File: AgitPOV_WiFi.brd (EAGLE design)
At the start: 36.2 x 66 mm, 33 parts

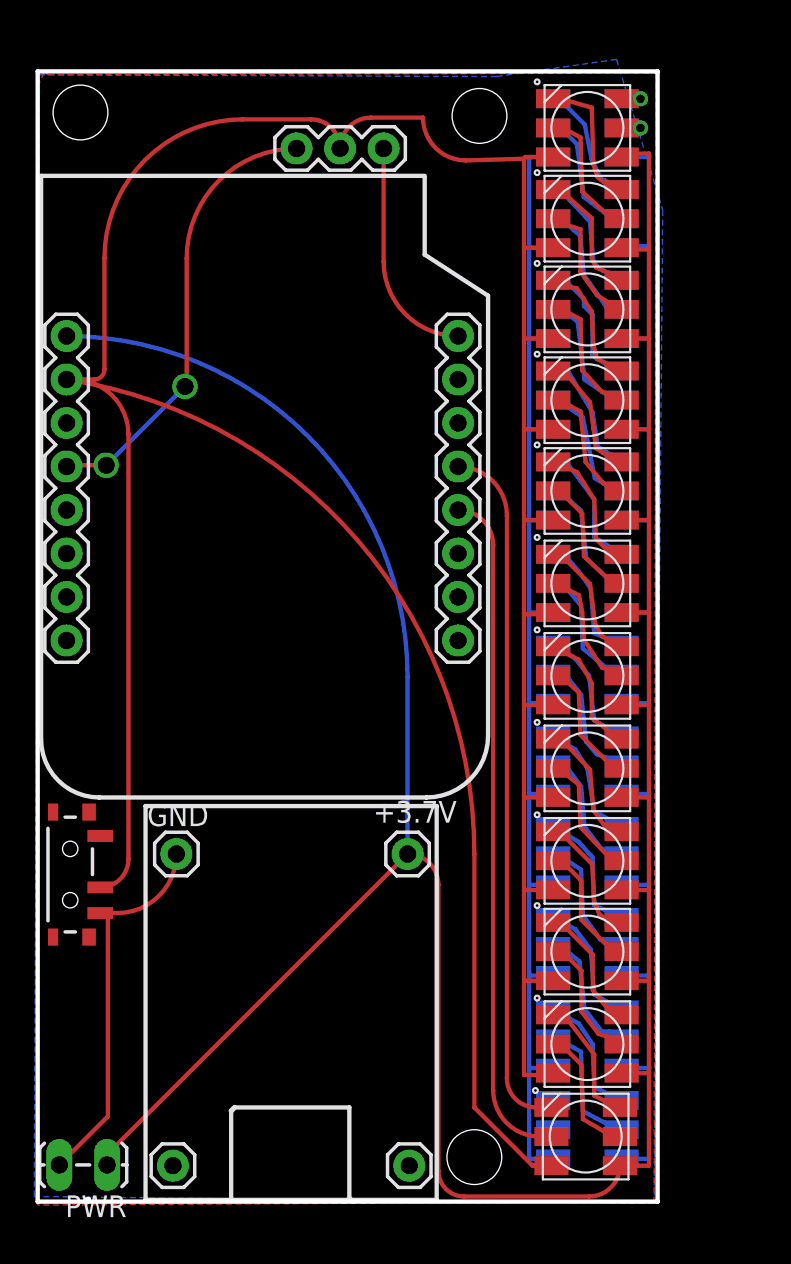
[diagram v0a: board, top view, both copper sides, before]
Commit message: With an option (untested) of an accelerometer.
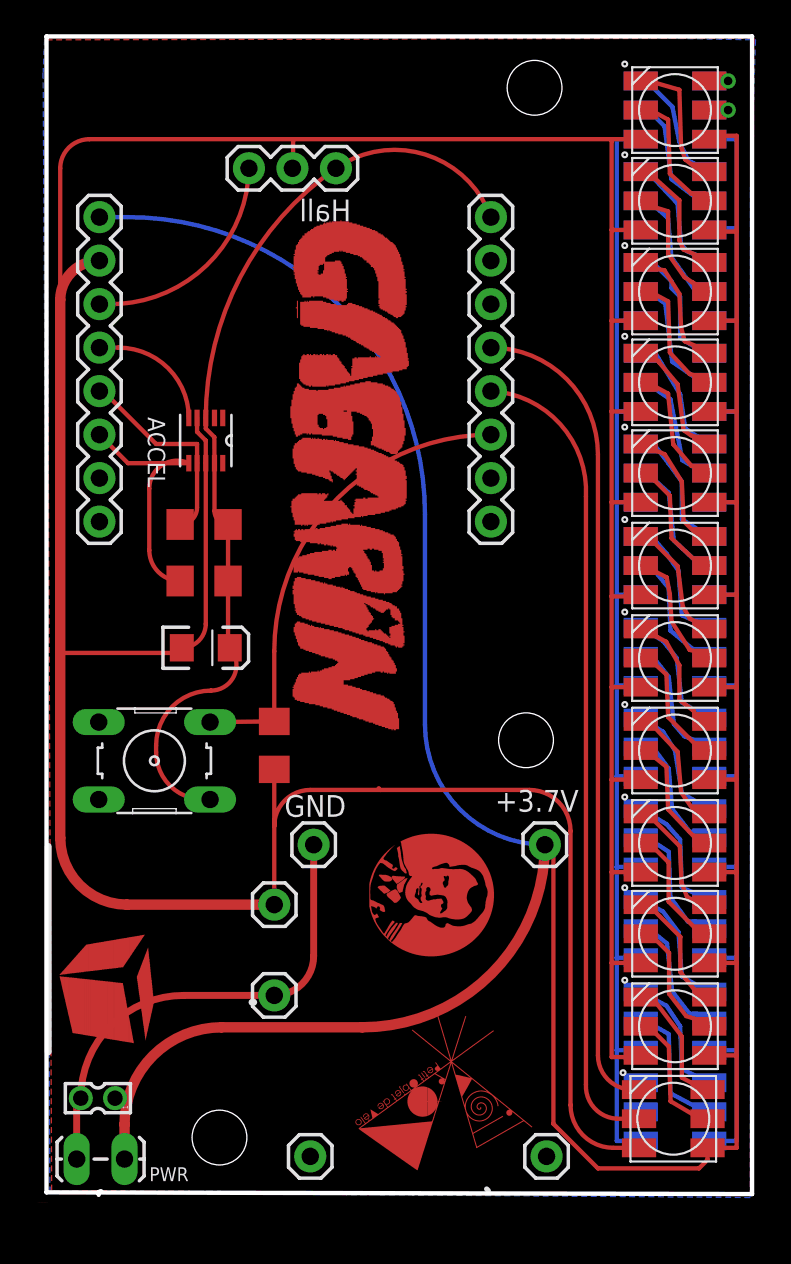
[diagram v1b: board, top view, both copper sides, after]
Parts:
- removed S1: (no value), SparkFun-Electromechanical:SWITCH-SPST-SMD-A
- added ACCEL: MMA7660FCT, Freescale_By_element14_Batch_1:DFN300X300X100-10N
- added C1: 0.1uF, SparkFun-Capacitors:EIA3216
- added JP3: SWITCH, SparkFun-Connectors:1X01
- added JP4: -, SparkFun-Connectors:1X01
- added JST: 332-02, con-garry:332-02
- added PUSHBUTTON: (no value), switch-omron:B3F-10XX
- added R1, R2: 4.7k, SparkFun-Resistors:1206
- added R3: 10k, SparkFun-Resistors:1206
- moved PIN0 8.03 mm to (29.7, 2.64)
- moved GND 8.03 mm to (16.1, 20.8)
- moved KK 8.03 mm to (15.9, 2.64)
- moved +3.7V 8.03 mm to (29.6, 20.8)
- moved WEMOS1 7.20 mm to (26.5, 39.7)
- moved WEMOS2 7.20 mm to (3.61, 57.5)
- moved DEL1 5.22 mm to (37.1, 4.84)
- moved DEL11 5.22 mm to (37.2, 58.4)
- moved DEL16 5.22 mm to (37.2, 47.8)
- moved DEL19 5.22 mm to (37.2, 31.8)
- moved DEL2 5.22 mm to (37.2, 10.2)
- moved DEL20 5.22 mm to (37.2, 26.5)
- moved DEL21 5.22 mm to (37.2, 21.2)
- moved DEL22 5.22 mm to (37.2, 15.9)
- moved DEL23 5.22 mm to (37.2, 10.5)
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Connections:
- removed net CH_PD: HALL.1, WEMOS1.8
- removed net D3: HALL.3, WEMOS2.4
- new net +3.3V: ACCEL.3, ACCEL.9, C1.A, HALL.1, PUSHBUTTON.1, R1.2, R2.2, WEMOS1.8
- new net N$1: HALL.3, WEMOS2.3
- new net N$5: ACCEL.6, R2.1, WEMOS2.6
- new net N$65: ACCEL.7, R1.1, WEMOS2.5
- new net N$67: ACCEL.5, WEMOS2.4
- new net PULLDOWN: PUSHBUTTON.3, R3.2, WEMOS1.3
- net 5V: now also JST.1
- net GND: now also ACCEL.4, ACCEL.8, C1.C, JP3.1, R3.1; no longer S1.2
- net N$41: now also JP4.1, JST.2; no longer S1.1
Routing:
- net +3.3V: track 0.00 -> 51.9 mm
- net GND: track 201.0 -> 233.8 mm
- net PULLDOWN: track 0.00 -> 25.7 mm
- net D3: track 25.5 -> 0.00 mm, vias 2 -> 0
- net 5V: track 173.8 -> 191.3 mm
- net N$5: track 0.00 -> 14.8 mm
- net CH_PD: track 12.8 -> 0.00 mm
- net N$65: track 0.00 -> 12.1 mm
- net N$1: track 0.00 -> 11.9 mm
- net N$2: track 39.3 -> 46.6 mm
- net N$4: track 40.2 -> 47.1 mm
- net N$67: track 0.00 -> 6.92 mm
- net N$41: track 22.2 -> 27.3 mm
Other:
- board size 36.2 x 66 mm -> 41.2 x 67.6 mm
- board text added: "/Users/uqam/Documents/AgitPOV_WiFi/logo_texte_gagarin.bmp"
- board text added: "/Users/uqam/Documents/logos/logo_ohanda/ohanda_logo.bmp"
- board text added: "D0"
- board text added: "D1"
- board text removed: "/Users/uqam/Desktop/Artengine_logo_petit_n_b.bmp"
- board text removed: "/Users/uqam/Desktop/cociclo_logo.bmp"

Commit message: Tout à sa place
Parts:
- removed +3.7V: (no value), SparkFun-Connectors:1X01
- removed JP3: SWITCH, SparkFun-Connectors:1X01
- removed JP4: -, SparkFun-Connectors:1X01
- removed PWR: (no value), SparkFun-Connectors:1X02_LOCK_LONGPADS
- added BATT: (no value), SparkFun-Connectors:1X02_LOCK_LONGPADS
- added BATT+: (no value), SparkFun-Connectors:1X01
- added JP-GND: SWITCH, SparkFun-Connectors:1X01
- added JP-GNDE: -, SparkFun-Connectors:1X01
- moved JST 1.81 mm to (3.40, 7.84), flipped to the bottom
- moved WEMOS1 0.26 mm to (26.3, 39.5)
- moved ACCEL 0.26 mm to (9.65, 44.2)
- moved DEL11 0.26 mm to (37.1, 58.2)
- moved FFFFF 0.26 mm to (37.1, 58.2)
- moved GND 0.26 mm to (16.0, 20.6)
- moved PIN0 0.26 mm to (29.6, 2.44)
- moved DEL19 0.26 mm to (37.1, 31.6)
- moved DEL20 0.26 mm to (37.1, 26.3)
- moved DEL5 0.26 mm to (37.1, 26.1)
- moved R3 0.26 mm to (13.7, 26.4)
- moved KK 0.26 mm to (15.8, 2.44)
- moved HALL 0.26 mm to (17.3, 60.1)
- moved DEL1 0.26 mm to (37.0, 4.64)
- moved DEL2 0.26 mm to (37.1, 10.0)
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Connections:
- removed net 5V1: DEL13.1, DEL15.1, DEL16.1, DEL17.1, DEL18.1, DEL19.1, DEL20.1, DEL21.1, DEL22.1, DEL23.1, DEL24.1, FFFFF.1
- removed net GND1: DEL13.6, DEL15.6, DEL16.6, DEL17.6, DEL18.6, DEL19.6, DEL20.6, DEL21.6, DEL22.6, DEL23.6, DEL24.6, FFFFF.6
- removed net N$41: GND.1, JP4.1, JST.2, PWR.2
- new net ENTREEGND: BATT.1, GND.1, JP-GNDE.1, JST.1
- net 5V: now also BATT+.1, BATT.2, DEL13.1, DEL15.1, DEL16.1, DEL17.1, DEL18.1, DEL19.1, DEL20.1, DEL21.1, DEL22.1, DEL23.1, DEL24.1, FFFFF.1, JST.2; no longer +3.7V.1, JST.1, PWR.1
- net GND: now also DEL13.6, DEL15.6, DEL16.6, DEL17.6, DEL18.6, DEL19.6, DEL20.6, DEL21.6, DEL22.6, DEL23.6, DEL24.6, FFFFF.6, JP-GND.1; no longer JP3.1
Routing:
- net 5V: track 191.3 -> 288.4 mm
- net GND1: track 79.3 -> 0.00 mm
- net GND: track 233.8 -> 312.5 mm
- net 5V1: track 75.3 -> 0.00 mm
- net ENTREEGND: track 0.00 -> 28.0 mm
- net N$41: track 27.3 -> 0.00 mm
- net +3.3V: track 51.9 -> 44.7 mm
- net PULLDOWN: track 25.7 -> 28.9 mm
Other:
- board text added: "BATT+"
- board text added: "C1"
- board text added: "R1"
- board text added: "R2"
- board text added: "R3"
- board text removed: "+3.7V"
- board text removed: "/Users/uqam/Documents/logos/logo_ohanda/ohanda_logo.bmp"

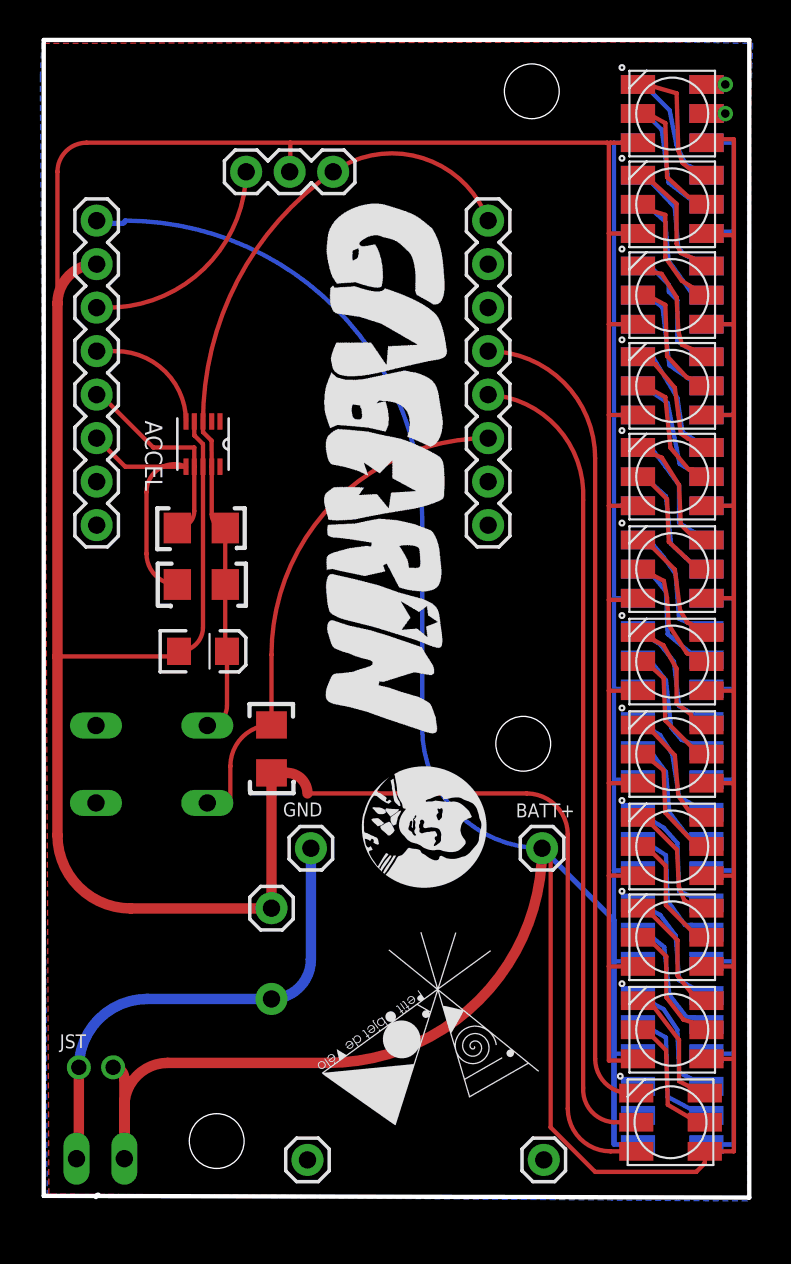
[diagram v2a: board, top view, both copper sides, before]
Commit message: added a capacitor for the accelerometer, DRChecked
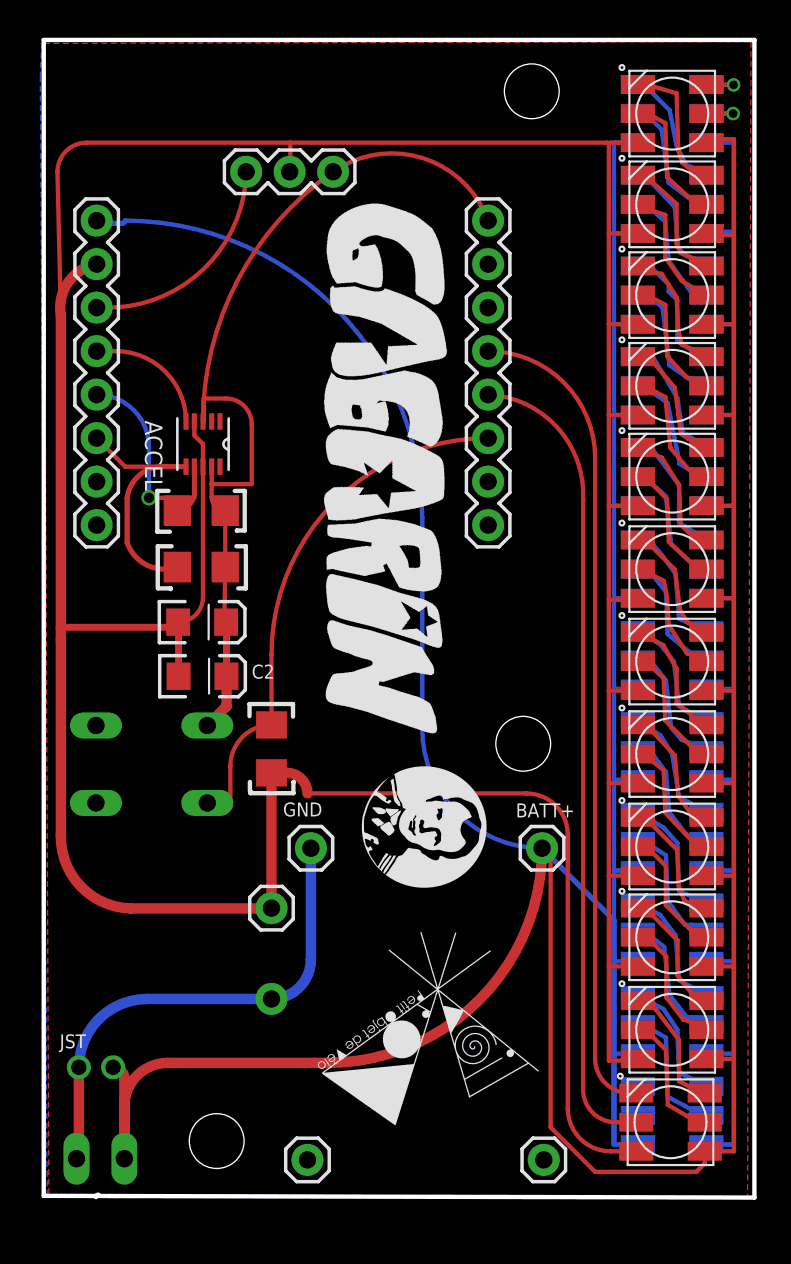
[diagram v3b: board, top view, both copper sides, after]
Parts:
- added C2: 0.1uF, SparkFun-Capacitors:EIA3216
- moved C1 1.70 mm to (9.60, 33.8)
- moved R1 1.02 mm to (9.55, 40.4)
- moved R2 1.02 mm to (9.55, 37.1)
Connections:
- net +3.3V: now also C2.A
- net GND: now also C2.C
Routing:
- net +3.3V: track 44.7 -> 52.5 mm
- net N$65: track 12.1 -> 14.7 mm, vias 0 -> 1
- net GND: track 312.5 -> 313.7 mm
- net N$5: track 14.8 -> 15.8 mm
- net N$42: track 2.20 -> 3.17 mm
- net N$8: track 2.20 -> 3.11 mm
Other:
- board size 41.2 x 67.6 mm -> 41.5 x 67.6 mm

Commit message: proper ACCEL integration
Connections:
- net GND: now also ACCEL.1
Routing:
- net GND: track 313.7 -> 340.4 mm, vias 0 -> 2
- net +3.3V: track 52.5 -> 63.9 mm
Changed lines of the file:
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@@
 <contactref element="ACCEL" pad="8"/>
 <contactref element="JP-GND" pad="1"/>
-<wire x1="9.14608125" y1="45.5577625" x2="9.14608125" y2="44.7449625" width="0.254" layer="1"/>
-<wire x1="9.14608125" y1="44.7449625" x2="9.65408125" y2="44.2369625" width="0.254" layer="1"/>
-<wire x1="9.65408125" y1="44.2369625" x2="9.65408125" y2="42.9161625" width="0.254" layer="1"/>
 <wire x1="1.35408125" y1="51.7549625" x2="1.35408125" y2="33.5387625" width="0.6096" layer="1"/>
-<wire x1="1.35408125" y1="33.5387625" x2="1.35408125" y2="32.8026" width="0.6096" layer="1"/>
-<wire x1="1.35408125" y1="32.8026" x2="1.35408125" y2="21.40111875" width="0.6096" layer="1"/>
+<wire x1="1.35408125" y1="33.5387625" x2="1.35408125" y2="21.40111875" width="0.6096" layer="1"/>
 <wire x1="8.20328125" y1="33.8387625" x2="8.50328125" y2="33.5387625" width="0.254" layer="1" curve="-90"/>
 <wire x1="33.35408125" y1="61.7369625" x2="33.25408125" y2="61.8369625" width="0.254" layer="1" curve="90"/>
@@
 <wire x1="1.35408125" y1="21.40111875" x2="5.4356" y2="17.1196" width="0.6096" layer="1" curve="90"/>
 <wire x1="3.44408125" y1="54.7449625" x2="1.35408125" y2="51.7549625" width="0.6096" layer="1" curve="90"/>
+<wire x1="9.14608125" y1="45.5577625" x2="9.15" y2="46.7" width="0.254" layer="1"/>
+<wire x1="9.15" y1="46.7" x2="14.71408125" y2="60.1369625" width="0.254" layer="1" curve="-44.594558"/>
+<contactref element="ACCEL" pad="1"/>
+<wire x1="39.05408125" y1="56.5369625" x2="35.05408125" y2="56.5369625" width="0" layer="19" extent="1-16"/>
+<wire x1="10.64468125" y1="45.5577625" x2="11.65" y2="46.56308125" width="0.254" layer="1" curve="90"/>
+<wire x1="11.65" y1="46.56308125" x2="11.65" y2="49.05" width="0.254" layer="1"/>
+<via x="11.65" y="49.05" extent="1-16" drill="0.6" shape="square"/>
+<wire x1="11.65" y1="49.05" x2="9.55" y2="51.15" width="0.254" layer="16" curve="90"/>
+<wire x1="9.55" y1="51.15" x2="8.45" y2="51.15" width="0.254" layer="16"/>
+<via x="8.45" y="51.15" extent="1-16" drill="0.6" shape="square"/>
+<wire x1="8.45" y1="51.15" x2="9.14608125" y2="50.45391875" width="0.254" layer="1" curve="-90"/>
+<wire x1="9.14608125" y1="50.45391875" x2="9.14608125" y2="45.5577625" width="0.254" layer="1"/>
 </signal>
 <signal name="+3.3V">
@@
 <wire x1="10.90328125" y1="33.9387625" x2="10.95408125" y2="37.0529625" width="0.254" layer="1"/>
 <wire x1="10.95408125" y1="37.0529625" x2="10.95408125" y2="40.3529625" width="0.254" layer="1"/>
-<wire x1="10.95408125" y1="40.3529625" x2="10.16208125" y2="41.1449625" width="0.254" layer="1" curve="-90"/>
-<wire x1="10.16208125" y1="41.1449625" x2="10.16208125" y2="41.9" width="0.254" layer="1"/>
 <contactref element="PUSHBUTTON" pad="1"/>
-<wire x1="10.16208125" y1="41.9" x2="10.16208125" y2="42.9161625" width="0.254" layer="1"/>
 <wire x1="9.65408125" y1="45.5577625" x2="17.25408125" y2="60.1369625" width="0.254" layer="1" curve="-55.065212"/>
 <wire x1="17.25408125" y1="60.1369625" x2="26.30408125" y2="57.2849625" width="0.254" layer="1" curve="-104.852826"/>
@@
 <wire x1="11.0266" y1="30.6832" x2="11.0266" y2="28.92291875" width="0.6096" layer="1"/>
 <wire x1="11.0266" y1="28.92291875" x2="9.90671875" y2="27.8030375" width="0.6096" layer="1"/>
-<wire x1="9.65408125" y1="45.5577625" x2="9.7" y2="45.60368125" width="0.254" layer="1" curve="90"/>
-<wire x1="9.7" y1="45.60368125" x2="9.7" y2="46.9" width="0.254" layer="1"/>
-<wire x1="9.7" y1="46.9" x2="11" y2="46.9" width="0.254" layer="1"/>
-<wire x1="11" y1="46.9" x2="12.5" y2="45.4" width="0.254" layer="1" curve="-90"/>
-<wire x1="12.5" y1="45.4" x2="12.5" y2="41.9" width="0.254" layer="1"/>
-<wire x1="12.5" y1="41.9" x2="10.16208125" y2="41.9" width="0.254" layer="1"/>
+<wire x1="10.95408125" y1="40.3529625" x2="12.6" y2="41.99888125" width="0.254" layer="1" curve="90"/>
+<wire x1="12.6" y1="41.99888125" x2="12.6" y2="50.75" width="0.254" layer="1"/>
+<wire x1="12.6" y1="50.75" x2="17.25408125" y2="60.1369625" width="0.254" layer="1" curve="-52.744681"/>
+<wire x1="12.6" y1="41.99888125" x2="10.16208125" y2="41.99888125" width="0.254" layer="1"/>
+<wire x1="10.16208125" y1="41.99888125" x2="10.16208125" y2="42.9161625" width="0.254" layer="1"/>
 </signal>
 <signal name="N$6">
